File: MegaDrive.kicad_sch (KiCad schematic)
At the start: 286 parts, among them J1 Video, J10 Conn_01x04_Pin, J11 Conn_01x02_Pin, J110 Conn_01x04_Pin, J111 Conn_01x02_Socket, J2 Floppy, J3 Cartridge, J4 EXT, J5 Player1, J6 Player2, J7 Jack-DC, J8 AudioJack3, J9 Conn_01x02_Pin, J99 Conn_01x02_Pin, SW1 SW_SPDT, SW2 SW_Push, U1 68000D, U10 M5M4C264L, U11 YM2612, U12 CXA1034P, U14 LM358, U15 L7805, U17 L7805, U2 uPD42832C-15, U3 uPD42832C-15, U6 Z80CPU, U7 uPD4364, U9 M5M4C264L

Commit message: use D-sub connctors that can be ordered
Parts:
- added H13, H14, H15: MountingHole, MountingHole:MountingHole_5mm, symbol Mechanical:MountingHole
- C1: footprint Capacitor_THT:CP_Radial_D8.0mm_P5.00mm -> Capacitor_THT:CP_Radial_Tantal_D4.5mm_P5.00mm
- J4: footprint Connector_Dsub:DSUB-9_Female_Horizontal_P2.77x2.54mm_EdgePinOffset9.40mm -> Connector_Dsub:DSUB-9_Female_Horizontal_P2.77x2.84mm_EdgePinOffset7.70mm_Housed_MountingHolesOffset9.12mm
- J5, J6: footprint Connector_Dsub:DSUB-9_Female_Horizontal_P2.77x2.54mm_EdgePinOffset9.40mm -> Connector_Dsub:DSUB-9_Male_Horizontal_P2.77x2.84mm_EdgePinOffset7.70mm_Housed_MountingHolesOffset9.12mm; symbol Connector:DE9_Receptacle -> Connector:DE9_Plug
- J7: footprint SEGA:DCJack -> SEGA:BarrelJack_CUI_PJ-002A_Horizontal
- U4: value ~ -> 315-5402
- U8: value ~ -> 312-5313A
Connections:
- net DCin1: now also J111.2 (Pin_2); no longer J111.1 (Pin_1)
- net DCin2: now also J111.1 (Pin_1); no longer J111.2 (Pin_2)
- net at J5.1: now also EM11.3; no longer EM5.3
- net at J5.2: now also EM12.3; no longer EM4.3
- net at J5.4: now also EM4.3; no longer EM12.3
- net at J5.5: now also EM5.3; no longer EM11.3
- net at J5.6: now also EM16.3; no longer R5.2
- net at J5.7: now also R4.2; no longer FB3.1
- net at J5.8: now also FB3.1; no longer R4.2
- net at J5.9: now also R5.2; no longer EM16.3
- net at EM26.3: now also J6.6; no longer J6.9
- net at J6.1: now also EM21.3; no longer EM25.3
- net at J6.2: now also EM22.3; no longer EM24.3
- net at J6.4: now also EM24.3; no longer EM22.3
- net at J6.5: now also EM25.3; no longer EM21.3
- net at R7.1: now also J6.9; no longer J6.6
- net at J6.7: now also R6.1; no longer FB4.1
- net at J6.8: now also FB4.1; no longer R6.1
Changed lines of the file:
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@@
     )
   )
-  (symbol (lib_id "Connector:DE9_Receptacle") (at 558.165 36.83 0) (unit 1)
+  (symbol (lib_id "Connector:DE9_Plug") (at 558.165 36.83 0) (unit 1)
     (in_bom yes) (on_board yes) (dnp no) (fields_autoplaced)
     (property "Reference" "J5" (at 563.88 35.56 0)
@@
       (effects (font (size 1.27 1.27)) (justify left))
     )
-    (property "Footprint" "Connector_Dsub:DSUB-9_Female_Horizontal_P2.77x2.54mm_EdgePinOffset9.40mm" (at 558.165 36.83 0)
+    (property "Footprint" "Connector_Dsub:DSUB-9_Male_Horizontal_P2.77x2.84mm_EdgePinOffset7.70mm_Housed_MountingHolesOffset9.12mm" (at 558.165 36.83 0)
       (effects (font (size 1.27 1.27)) hide)
     )
@@
       (effects (font (size 1.27 1.27)) (justify left))
     )
-    (property "Footprint" "Connector_Dsub:DSUB-9_Female_Horizontal_P2.77x2.54mm_EdgePinOffset9.40mm" (at 560.07 110.49 0)
+    (property "Footprint" "Connector_Dsub:DSUB-9_Female_Horizontal_P2.77x2.84mm_EdgePinOffset7.70mm_Housed_MountingHolesOffset9.12mm" (at 560.07 110.49 0)
       (effects (font (size 1.27 1.27)) hide)
     )
@@
   )
   (symbol (lib_id "SEGA:312-5313A") (at 53.975 240.665 0) (unit 1)
-    (in_bom yes) (on_board yes) (dnp no) (fields_autoplaced)
+    (in_bom yes) (on_board yes) (dnp no)
     (property "Reference" "U8" (at 57.4391 235.585 0)
       (effects (font (size 1.27 1.27)) (justify left))
     )
-    (property "Value" "~" (at 64.135 301.625 0)
+    (property "Value" "312-5313A" (at 62.865 233.045 0)
       (effects (font (size 1.27 1.27)))
     )
@@
       (effects (font (size 1.27 1.27)) (justify left))
     )
-    (property "Value" "~" (at 123.825 135.89 0)
+    (property "Value" "315-5402" (at 154.305 168.91 0)
       (effects (font (size 1.27 1.27)))
     )
@@
     )
   )
-  (symbol (lib_id "Connector:DE9_Receptacle") (at 559.435 74.93 0) (unit 1)
+  (symbol (lib_id "Connector:DE9_Plug") (at 559.435 74.93 0) (unit 1)
     (in_bom yes) (on_board yes) (dnp no) (fields_autoplaced)
     (property "Reference" "J6" (at 565.15 73.66 0)
@@
       (effects (font (size 1.27 1.27)) (justify left))
     )
-    (property "Footprint" "Connector_Dsub:DSUB-9_Female_Horizontal_P2.77x2.54mm_EdgePinOffset9.40mm" (at 559.435 74.93 0)
+    (property "Footprint" "Connector_Dsub:DSUB-9_Male_Horizontal_P2.77x2.84mm_EdgePinOffset7.70mm_Housed_MountingHolesOffset9.12mm" (at 559.435 74.93 0)
       (effects (font (size 1.27 1.27)) hide)
     )
@@
       (effects (font (size 1.27 1.27)))
     )
-    (property "Footprint" "SEGA:DCJack" (at 631.19 305.816 0)
+    (property "Footprint" "SEGA:BarrelJack_CUI_PJ-002A_Horizontal" (at 631.19 305.816 0)
       (effects (font (size 1.27 1.27)) hide)
     )
@@
     )
   )
+  (symbol (lib_id "Mechanical:MountingHole") (at 587.375 355.6 0) (unit 1)
+    (in_bom yes) (on_board yes) (dnp no) (fields_autoplaced)
+    (property "Reference" "H14" (at 590.55 354.33 0)
+      (effects (font (size 1.27 1.27)) (justify left))
+    )
+    (property "Value" "MountingHole" (at 590.55 356.87 0)
+      (effects (font (size 1.27 1.27)) (justify left))
+    )
+    (property "Footprint" "MountingHole:MountingHole_5mm" (at 587.375 355.6 0)
+      (effects (font (size 1.27 1.27)) hide)
+    )
+    (property "Datasheet" "~" (at 587.375 355.6 0)
+      (effects (font (size 1.27 1.27)) hide)
+    )
+    (instances
+      (project "MegaDrive"
+        (path "/71502cc5-74ca-49c7-88ef-27b9c9d4628d"
+          (reference "H14") (unit 1)
+        )
+      )
+    )
+  )
   (symbol (lib_id "power:VCCQ") (at 458.47 26.67 90) (unit 1)
     (in_bom yes) (on_board yes) (dnp no) (fields_autoplaced)
@@
     )
   )
+  (symbol (lib_id "Mechanical:MountingHole") (at 587.375 350.52 0) (unit 1)
+    (in_bom yes) (on_board yes) (dnp no) (fields_autoplaced)
+    (property "Reference" "H13" (at 590.55 349.25 0)
+      (effects (font (size 1.27 1.27)) (justify left))
+    )
+    (property "Value" "MountingHole" (at 590.55 351.79 0)
+      (effects (font (size 1.27 1.27)) (justify left))
+    )
+    (property "Footprint" "MountingHole:MountingHole_5mm" (at 587.375 350.52 0)
+      (effects (font (size 1.27 1.27)) hide)
+    )
+    (property "Datasheet" "~" (at 587.375 350.52 0)
+      (effects (font (size 1.27 1.27)) hide)
+    )
+    (instances
+      (project "MegaDrive"
+        (path "/71502cc5-74ca-49c7-88ef-27b9c9d4628d"
+          (reference "H13") (unit 1)
+        )
+      )
+    )
+  )
   (symbol (lib_id "Device:R") (at 323.85 356.235 180) (unit 1)
     (in_bom yes) (on_board yes) (dnp no) (fields_autoplaced)
@@
       (effects (font (size 1.27 1.27)) (justify right))
     )
-    (property "Footprint" "Capacitor_THT:CP_Radial_D8.0mm_P5.00mm" (at 705.1548 290.83 0)
+    (property "Footprint" "Capacitor_THT:CP_Radial_Tantal_D4.5mm_P5.00mm" (at 705.1548 290.83 0)
       (effects (font (size 1.27 1.27)) hide)
     )
@@
     )
   )
-  (symbol (lib_id "Connector:Conn_01x02_Socket") (at 642.62 303.53 0) (unit 1)
-    (in_bom yes) (on_board yes) (dnp no) (fields_autoplaced)
-    (property "Reference" "J111" (at 644.525 303.53 0)
+  (symbol (lib_id "Connector:Conn_01x02_Socket") (at 642.62 306.07 0) (mirror x) (unit 1)
+    (in_bom yes) (on_board yes) (dnp no)
+    (property "Reference" "J111" (at 644.525 306.07 0)
       (effects (font (size 1.27 1.27)) (justify left))
     )
-    (property "Value" "Conn_01x02_Socket" (at 644.525 306.07 0)
+    (property "Value" "Conn_01x02_Socket" (at 644.525 303.53 0)
       (effects (font (size 1.27 1.27)) (justify left))
     )
-    (property "Footprint" "Connector_PinHeader_2.54mm:PinHeader_1x02_P2.54mm_Vertical" (at 642.62 303.53 0)
+    (property "Footprint" "Connector_PinHeader_2.54mm:PinHeader_1x02_P2.54mm_Vertical" (at 642.62 306.07 0)
       (effects (font (size 1.27 1.27)) hide)
     )
-    (property "Datasheet" "~" (at 642.62 303.53 0)
+    (property "Datasheet" "~" (at 642.62 306.07 0)
       (effects (font (size 1.27 1.27)) hide)
     )
@@
         )
       )
+    )
+  )
+  (symbol (lib_id "Mechanical:MountingHole") (at 587.375 360.68 0) (unit 1)
+    (in_bom yes) (on_board yes) (dnp no) (fields_autoplaced)
+    (property "Reference" "H15" (at 590.55 359.41 0)
+      (effects (font (size 1.27 1.27)) (justify left))
+    )
+    (property "Value" "MountingHole" (at 590.55 361.95 0)
+      (effects (font (size 1.27 1.27)) (justify left))
+    )
+    (property "Footprint" "MountingHole:MountingHole_5mm" (at 587.375 360.68 0)
+      (effects (font (size 1.27 1.27)) hide)
+    )
+    (property "Datasheet" "~" (at 587.375 360.68 0)
+      (effects (font (size 1.27 1.27)) hide)
+    )
+    (instances
+      (project "MegaDrive"
+        (path "/71502cc5-74ca-49c7-88ef-27b9c9d4628d"
+          (reference "H15") (unit 1)
+        )
+      )

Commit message: missing resistor and bom fixup
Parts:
- added R31: 2.2k, Resistor_SMD:R_0805_2012Metric, symbol Device:R
- C11, C75: value 0,01uF -> 10nF
- C112, C29, C92: value 33p -> 33pF
- C118: now not fitted; now left out of the parts list
- C121: value 0,1uF -> 100nF
- C2, C3, C73, C83: value C -> 22nF
- C25, C26, C27, C28: value 22n -> 22nF
- C45: value C -> 0.1uF
- C78: value 47 -> 33pF
- C81: value 220p -> 220pF
- C82: value 20p -> 20pF
- C85: value 100pF -> 1000pF
- C87: value 0.022u -> 22nF
- C88: value 47 -> 47pF
- C89: value 0,01uF -> 22nF
- D3: value D -> ISR35-100A
- L2, L3, L7: value 100mH -> 100uH
- L5: value 12mH -> 12uH
- L6: value L -> 0; now left out of the parts list
- R1: value 4.7k -> 47k
- R36, R39, R52: value R -> 47k
- R4, R5, R6, R7: value R -> 330
- R49: value R -> 75
- renumbered R13 to R32
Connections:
- net GND: now also R31.2
- net at C39.1, C40.2, U8.95 (SOUND): now also R31.1
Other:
- moved on the sheet: C106, C109, C78, C81

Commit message: fix some cap values and probably mess some up
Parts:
- C102, C103, C105, C106, C107, C108, C109, C110, C112, C113, C115, C116, C117, C120, C14, C16, C17, C18, C20, C21, C22, C29, C6, C78, C90, C92: value 33pF -> 22pF
- C19: value 22pF -> 22nF
- C2, C3, C73, C83: value 22nF -> 0.1uF
- FB7: value FerriteBead -> 4T Radial
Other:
- moved on the sheet: C1, C121, C2, C3, C73, C74, C79, C83, D1, D3, FB1, FB2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

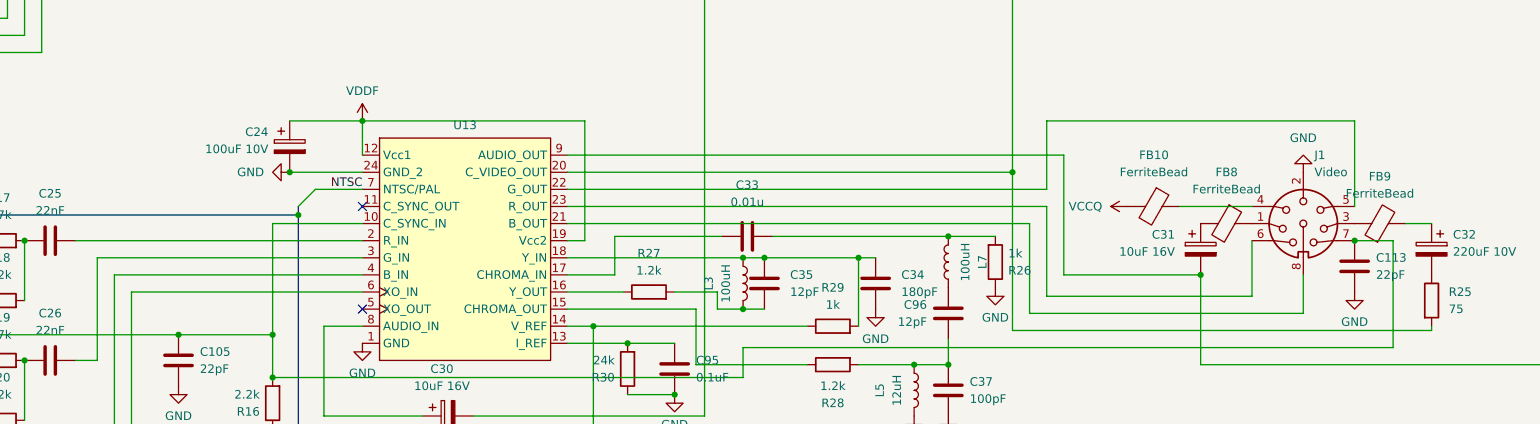
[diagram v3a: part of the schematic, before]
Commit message: add silkscreen so no one else rotates their vdp
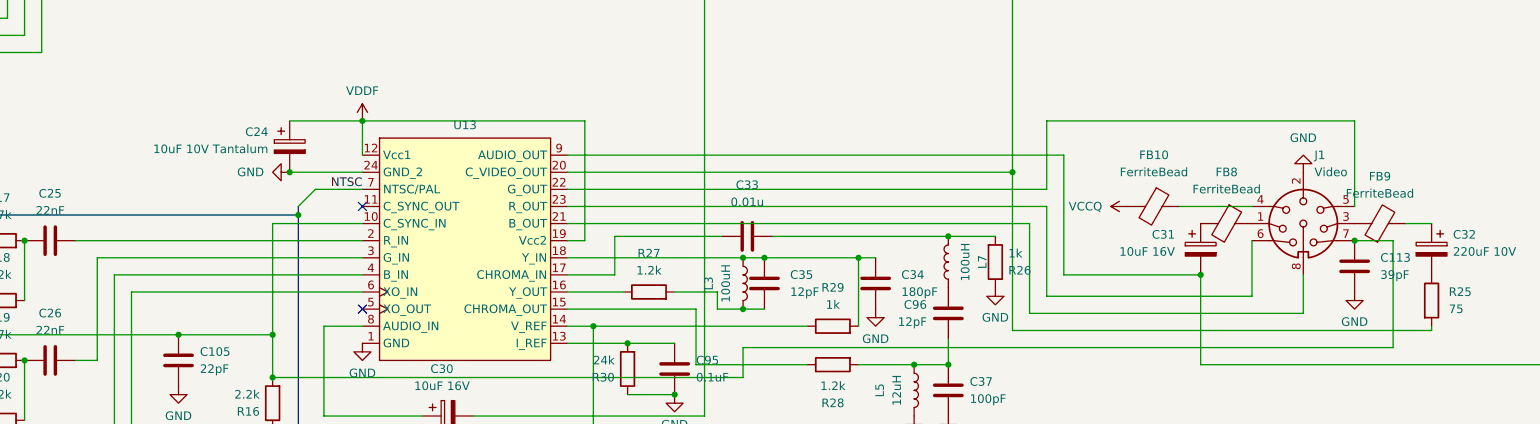
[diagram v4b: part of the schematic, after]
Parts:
- C113: value 22pF -> 39pF
- C24: value 100uF 10V -> 10uF 10V Tantalum
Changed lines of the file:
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@@
       (effects (font (size 1.27 1.27)) (justify right))
     )
-    (property "Value" "100uF 10V" (at 224.79 399.796 0)
+    (property "Value" "10uF 10V Tantalum" (at 224.79 399.796 0)
       (effects (font (size 1.27 1.27)) (justify right))
     )
@@
   (symbol (lib_id "Device:C") (at 386.08 417.195 0) (unit 1)
     (in_bom yes) (on_board yes) (dnp no) (fields_autoplaced)
-    (property "Reference" "C113" (at 389.255 415.925 0)
-      (effects (font (size 1.27 1.27)) (justify left))
-    )
-    (property "Value" "22pF" (at 389.255 418.465 0)
-      (effects (font (size 1.27 1.27)) (justify left))
-    )
+    (property "Reference" "C113" (at 389.89 415.925 0)
+      (effects (font (size 1.27 1.27)) (justify left))
+    )
+    (property "Value" "39pF" (at 389.89 418.465 0)
+      (effects (font (size 1.27 1.27)) (justify left))
+    )

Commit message: missing zclk connection
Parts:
- added NT101: NetTie_2, NetTie:NetTie-2_SMD_Pad2.0mm, symbol Device:NetTie_2
- J4: footprint Connector_Dsub:DSUB-9_Female_Horizontal_P2.77x2.84mm_EdgePinOffset7.70mm_Housed_MountingHolesOffset9.12mm -> Connector_Dsub:DSUB-9_Socket_Horizontal_P2.77x2.84mm_EdgePinOffset9.40mm; symbol Connector:DE9_Receptacle -> Connector:DE9_Socket
- J5, J6: footprint Connector_Dsub:DSUB-9_Male_Horizontal_P2.77x2.84mm_EdgePinOffset7.70mm_Housed_MountingHolesOffset9.12mm -> Connector_Dsub:DSUB-9_Pins_Horizontal_P2.77x2.84mm_EdgePinOffset9.40mm; symbol Connector:DE9_Plug -> Connector:DE9_Pins
- U1: value 68000D -> HD68HC000P8; symbol CPU_NXP_68000:68000D -> CPU_NXP_68000:MC68000P
- U4: footprint Package_QFP:PQFP-160_28x28mm_P0.65mm -> SEGA:QFP-160_28x28_Pitch0.65mm
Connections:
- net VCCQ: now also NT101.1; no longer C16.1, C24.1, L6.1, R55.1, R56.1, R57.1, U13.12 (Vcc1), U13.19 (Vcc2), U8.30 (AVC)
- net ZCLK: now also C88.1, U8.51 (CLK0)
- net ~{HALT}: now reaches U1.17 (~{HALT}), U4.133 (~{HALT})
- net ~{VPA}: now reaches U1.21 (~{VPA}), U4.135 (~{VPA})
- new net VDDF: C16.1, C24.1, L6.1, NT101.2, R55.1, R56.1, R57.1, U13.12 (Vcc1), U13.19 (Vcc2), U8.30 (AVC)
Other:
- moved on the sheet: C1, C10, C102, C103, C105, C106, C107, C108, C109, C11, C110, C111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
